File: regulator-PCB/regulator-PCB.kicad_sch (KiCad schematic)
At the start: 95 parts, among them J1 Conn_ARM_SWD_TagConnect_TC2030, J10 Conn_01x01_Pin, J2 PJ-059A, J3 Conn_01x01_Pin, J4 Conn_01x01_Pin, J5 Conn_01x01_Pin, J6 Conn_01x01_Pin, J7 Conn_01x01_Pin, J8 Conn_01x01_Pin, J9 Conn_01x01_Pin, Q1 2N3904, Q10 2N3904, Q11 2N3904, Q12 2N3904, Q13 2N3904, Q14 2N3904, Q15 2N3904, Q2 2N3904, Q3 2N3904, Q4 2N3904, Q5 2N3904, Q6 2N3904, Q7 2N3904, Q8 2N3904, Q9 2N3904, U1 STM32C092KCT6, U10 LH1546AT, U11 LH1546AT, U12 LH1546AT, U13 LH1546AT, U14 LH1546AT, U15 LH1546AT, U16 LH1546AT, U17 LH1546AT, U2 LP2985-3.3, U3 LH1546AT, U4 LH1546AT, U5 LH1546AT, U6 LH1546AT, U7 LH1546AT, U8 LH1546AT, U9 LH1546AT

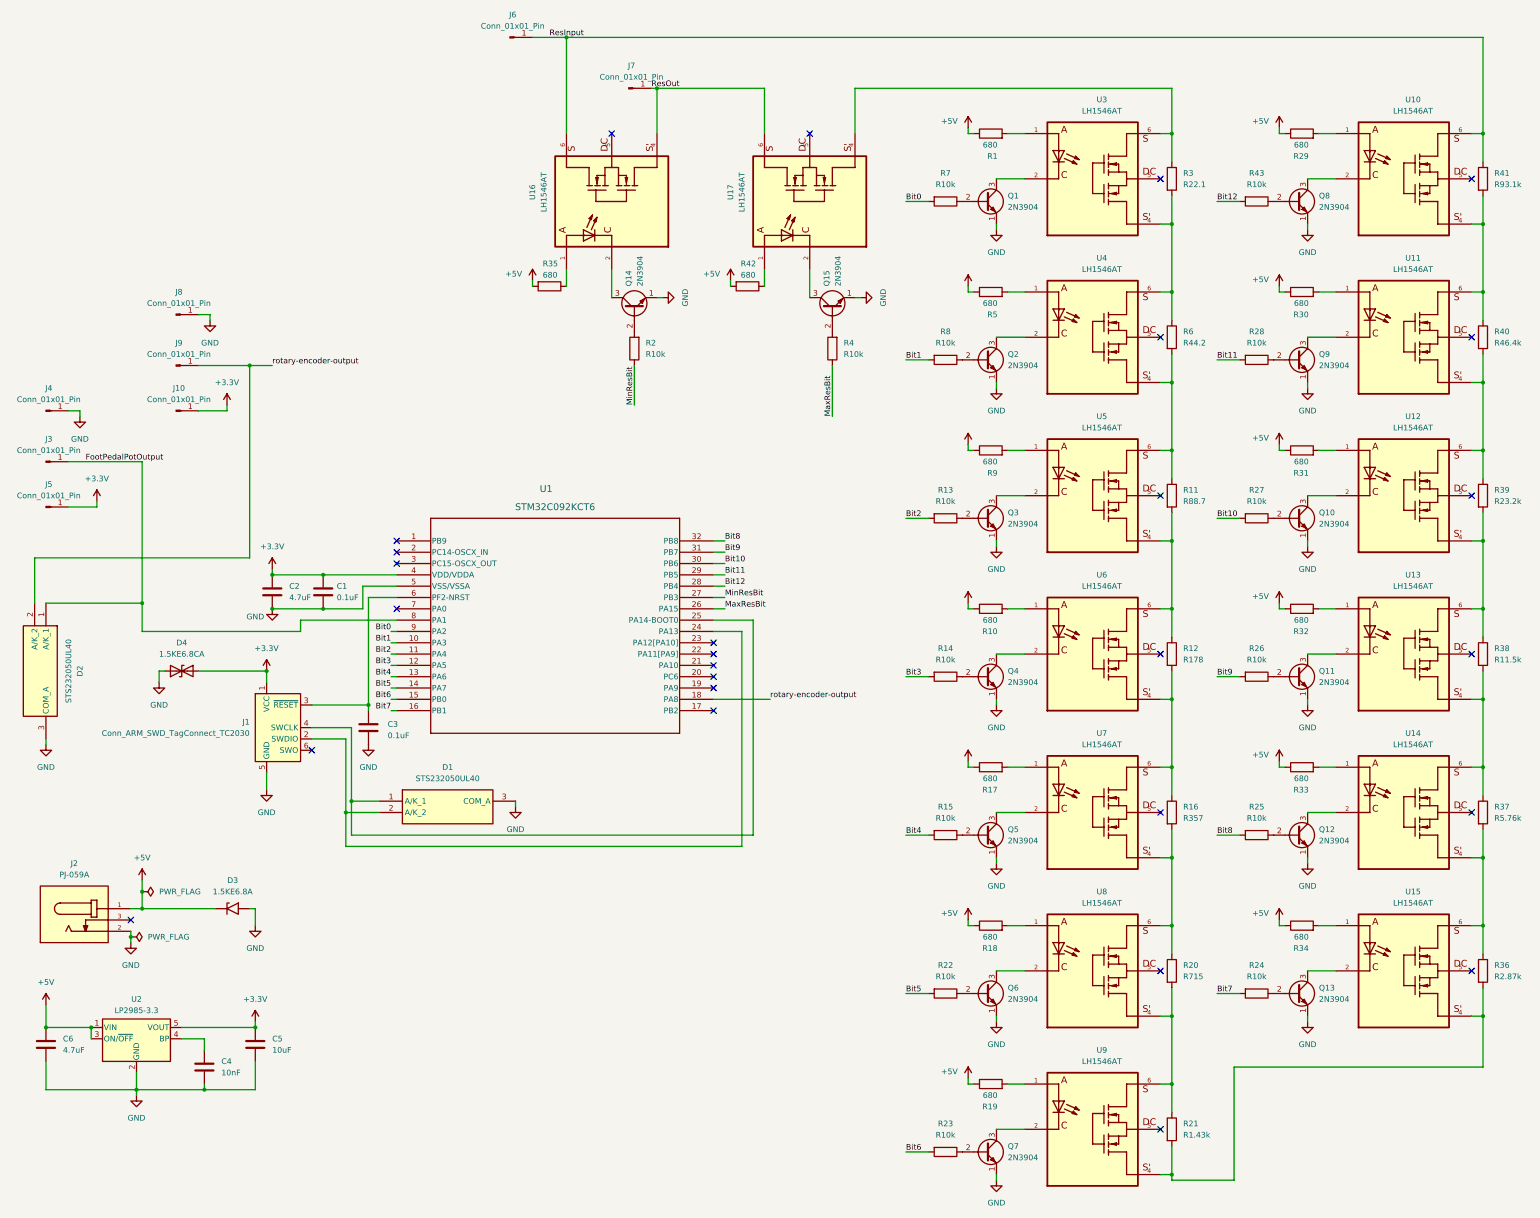
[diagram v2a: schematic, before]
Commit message: Regular PCB schematic completed. Drafted a poor design for the regulator PCB, then added line voltage safety constraints. Pending PCB redesign.
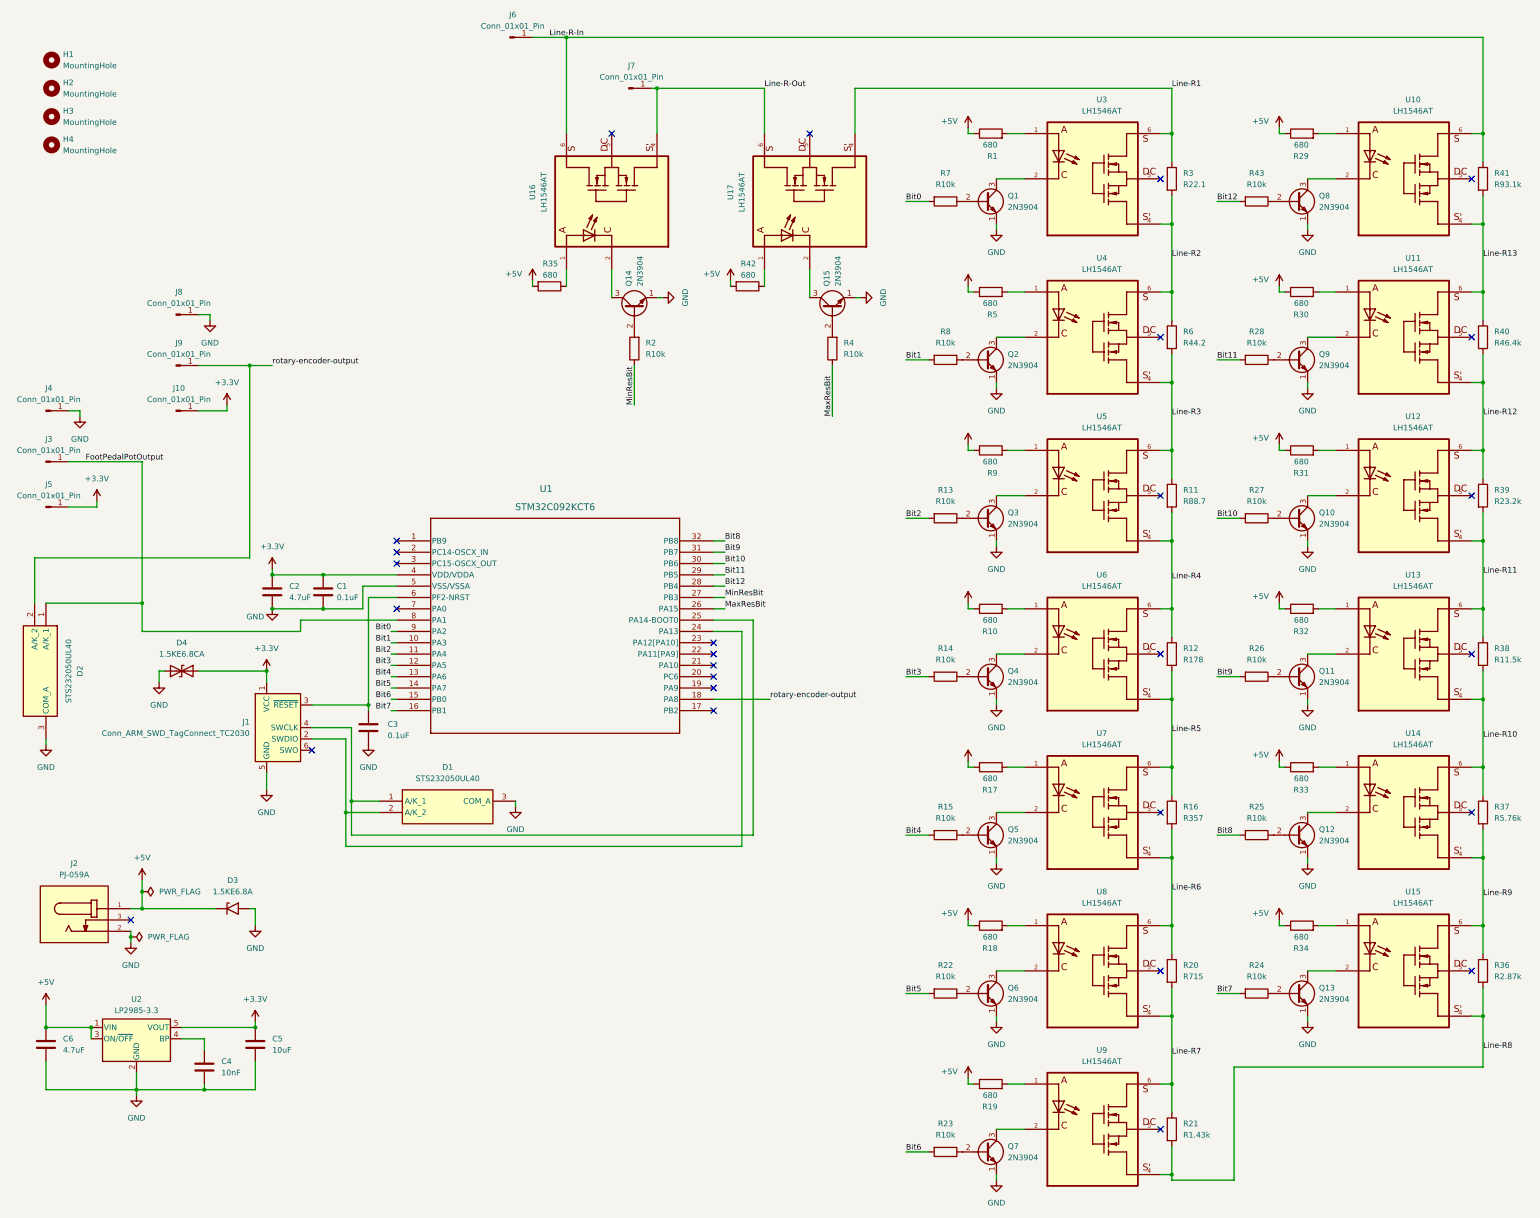
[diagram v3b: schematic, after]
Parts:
- added H1, H2, H3, H4: MountingHole, MountingHole:MountingHole_4.5mm, symbol Mechanical:MountingHole
- J10, J3, J4, J5, J6, J7, J8, J9: footprint Connector_Wire:SolderWire-0.5sqmm_1x01_D0.9mm_OD2.3mm_Relief2x -> Connector_Wire:SolderWire-0.75sqmm_1x01_D1.25mm_OD2.3mm_Relief
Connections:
- net Line-R9: now reaches R36.1, R37.2, U14.4, U15.6
- net Line-R8: now reaches R21.2, R36.2, U15.4, U9.4
- net Line-R11: now reaches R38.1, R39.2, U12.4, U13.6
- net Line-R12: now reaches R39.1, R40.2, U11.4, U12.6
- net Line-R7: now reaches R20.2, R21.1, U8.4, U9.6
- net Line-R3: now reaches R11.1, R6.2, U4.4, U5.6
- net Line-R4: now reaches R11.2, R12.1, U5.4, U6.6
- net Line-R6: now reaches R16.2, R20.1, U7.4, U8.6
- net Line-R13: now reaches R40.1, R41.2, U10.4, U11.6
- net Line-R5: now reaches R12.2, R16.1, U6.4, U7.6
- net Line-R1: now reaches R3.1, U17.4, U3.6
- net Line-R2: now reaches R3.2, R6.1, U3.4, U4.6
- net Line-R10: now reaches R37.1, R38.2, U13.4, U14.6
- net ResInput renamed Line-R-In
- net ResOut renamed Line-R-Out

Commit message: Regulator PCB v1.0 designed and ordered.
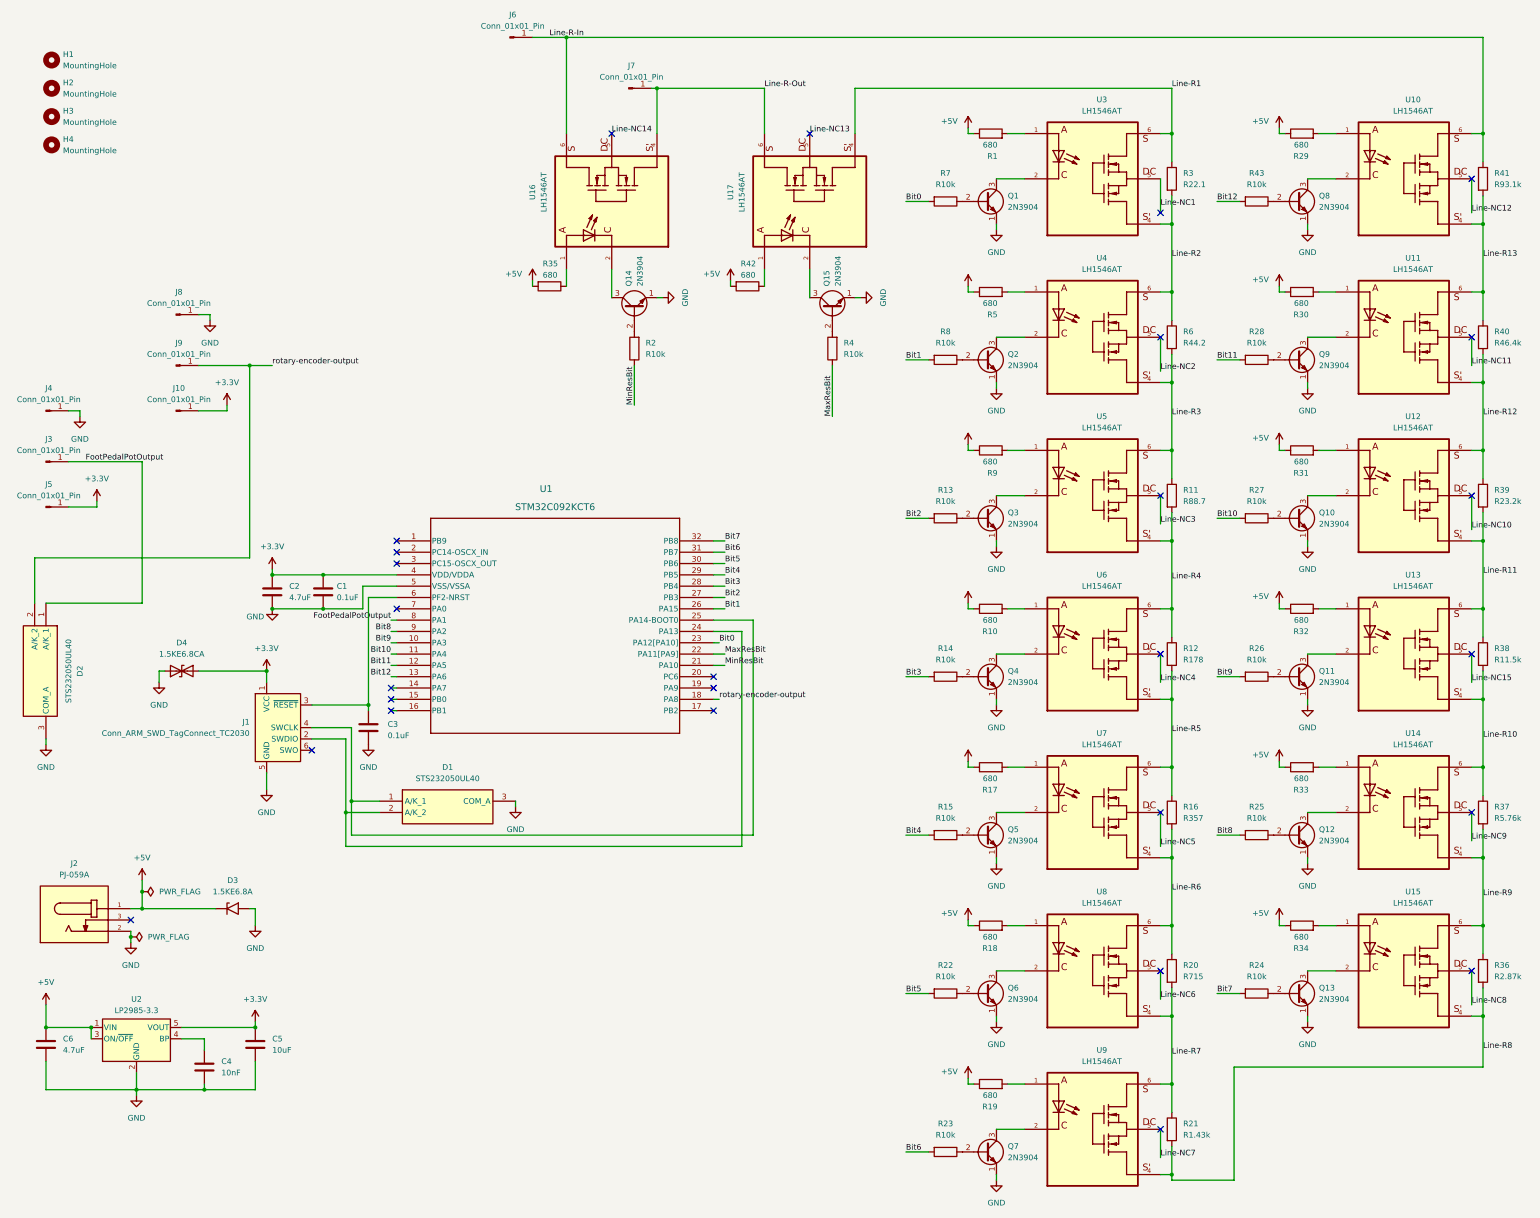
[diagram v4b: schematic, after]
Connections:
- net Bit0: now also U1.23 (PA12[PA10]); no longer U1.9 (PA2)
- net Bit1: now also U1.26 (PA15); no longer U1.10 (PA3)
- net Bit10: now also U1.11 (PA4); no longer U1.30 (PB6)
- net Bit11: now also U1.12 (PA5); no longer U1.29 (PB5)
- net Bit12: now also U1.13 (PA6); no longer U1.28 (PB4)
- net Bit2: now also U1.27 (PB3); no longer U1.11 (PA4)
- net Bit3: now also U1.28 (PB4); no longer U1.12 (PA5)
- net Bit4: now also U1.29 (PB5); no longer U1.13 (PA6)
- net Bit5: now also U1.30 (PB6); no longer U1.14 (PA7)
- net Bit6: now also U1.31 (PB7); no longer U1.15 (PB0)
- net Bit7: now also U1.32 (PB8); no longer U1.16 (PB1)
- net Bit8: now also U1.9 (PA2); no longer U1.32 (PB8)
- net Bit9: now also U1.10 (PA3); no longer U1.31 (PB7)
- net MaxResBit: now also U1.22 (PA11[PA9]); no longer U1.26 (PA15)
- net MinResBit: now also U1.21 (PA10); no longer U1.27 (PB3)
- net Line-NC10: now reaches U12.5
- net Line-NC7: now reaches U9.5
- net Line-NC6: now reaches U8.5
- net Line-NC12: now reaches U10.5
- net Line-NC14: now reaches U16.5
- net Line-NC13: now reaches U17.5
- net Line-NC3: now reaches U5.5
- net Line-NC9: now reaches U14.5
- net Line-NC15: now reaches U13.5
- net Line-NC5: now reaches U7.5
- net Line-NC4: now reaches U6.5
- net Line-NC11: now reaches U11.5
- net Line-NC1: now reaches U3.5
- net Line-NC8: now reaches U15.5
- net Line-NC2: now reaches U4.5
